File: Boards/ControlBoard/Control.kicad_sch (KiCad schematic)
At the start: 20 parts, among them J29 Conn_01x02_Pin

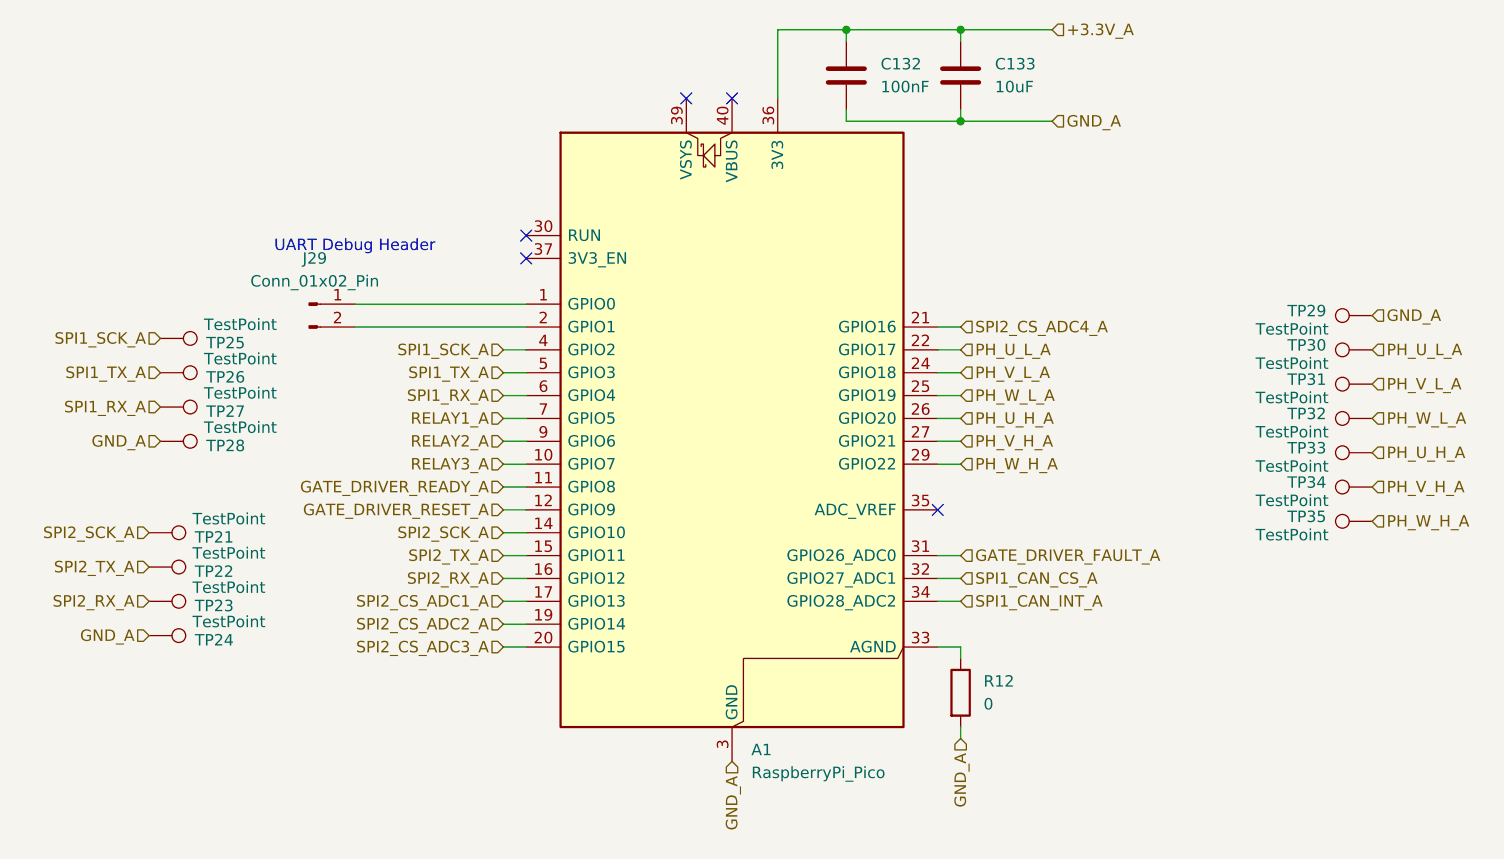
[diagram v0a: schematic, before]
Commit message: Layout controlboard, update cad
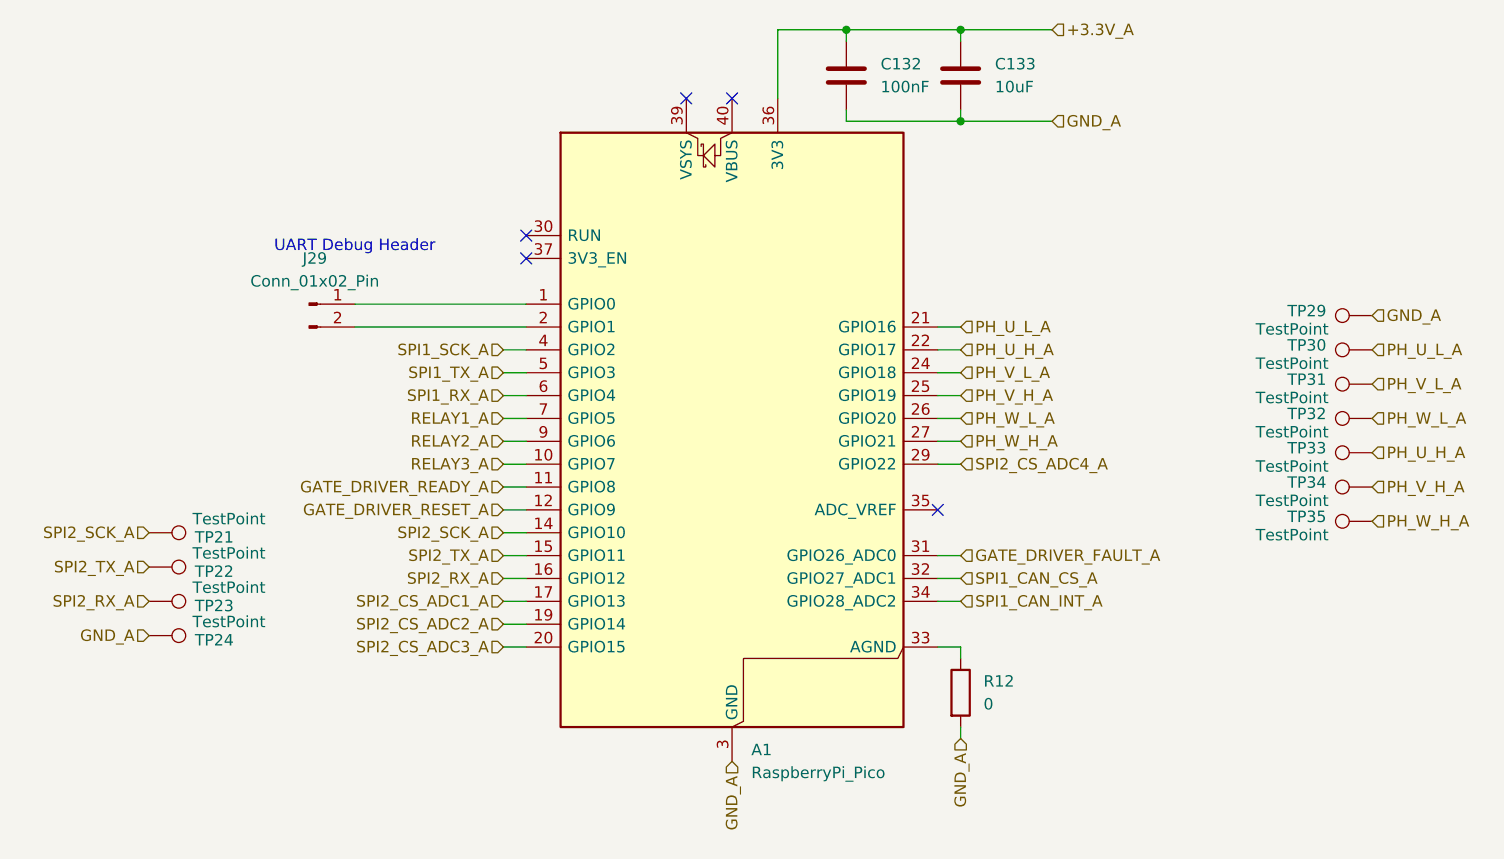
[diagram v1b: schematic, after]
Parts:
- removed TP25, TP26, TP27, TP28: TestPoint, TestPoint:TestPoint_Loop_D2.54mm_Drill1.5mm_Beaded, symbol Connector:TestPoint
- A1: footprint InverterCom:RaspberryPi_Pico_Common_Unspecified -> Module:RaspberryPi_Pico_Common_THT
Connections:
- net PH_U_H_A: now also A1.22 (GPIO17); no longer A1.26 (GPIO20)
- net PH_U_L_A: now also A1.21 (GPIO16); no longer A1.22 (GPIO17)
- net PH_V_H_A: now also A1.25 (GPIO19); no longer A1.27 (GPIO21)
- net PH_W_H_A: now also A1.27 (GPIO21); no longer A1.29 (GPIO22)
- net PH_W_L_A: now also A1.26 (GPIO20); no longer A1.25 (GPIO19)
- net SPI2_CS_ADC4_A: now also A1.29 (GPIO22); no longer A1.21 (GPIO16)
